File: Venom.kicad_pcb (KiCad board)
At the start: 2 copper layers, 72 x 42 mm, 38 parts, among them CN1 HC-XH-5A-G, CN2 HC-PH-8A-G, CN3 HC-XH-8A-G, CN4 HC-XH-8A-G, CN5 HC-XH-2A-G, CN6 HC-PH-7A-G, SW1 GT-TC030A-H020-L1N, SW2 GT-TC030A-H020-L1N, SW3 GT-TC030A-H020-L1N, U1 TLV73333PDBV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

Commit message: Potentially finished RP2040
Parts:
- moved SW1 27.1 mm to (106.7, 101.6)
- moved Y1 24.4 mm to (116.7, 96.0), turned to 180 degrees
- moved C2 16.5 mm to (119.4, 95.2), turned to -90 degrees
- moved C12 16.3 mm to (125.7, 101.6), turned to -90 degrees
- moved C13 15.5 mm to (125.7, 90.9), turned to 90 degrees
- moved C7 14.1 mm to (120.2, 98.7), turned to 180 degrees
- moved C3 13.7 mm to (116.8, 98.3)
- moved OSHW1 8.42 mm to (81.8, 95.6)
- moved C14 8.36 mm to (120.2, 97.7), turned to 180 degrees
- moved R5 5.62 mm to (119.8, 96.7), turned to 0 degrees
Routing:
- net +1V1: track 4.23 -> 34.2 mm, vias 1 -> 2
- net GND: track 27.9 -> 47.6 mm, vias 15 -> 20
- net +3V3: track 49.3 -> 55.3 mm
- net XIN: track 0.00 -> 4.05 mm
- net XOUT: track 0.00 -> 3.22 mm
- net Net-(C3-Pad1): track 0.00 -> 2.14 mm

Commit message: Nearly all wired up?
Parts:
- U2: value W25Q128JVS -> W25Q128JVSIQTR; footprint Package_SO:SOIC-8_5.23x5.23mm_P1.27mm -> easyeda2kicad:SOIC-8_L5.3-W5.3-P1.27-LS8.0-BL
- moved SW1 40.3 mm to (146.6, 106.8), turned to 180 degrees
- moved CN5 34.1 mm to (114.2, 80.0), turned to 90 degrees
- moved C12 7.82 mm to (119.3, 106.1), turned to 180 degrees
- moved CN3 4.69 mm to (98.7, 78.7)
- moved CN4 0.72 mm to (128.4, 78.7)
- moved C13 0.66 mm to (125.4, 90.3)
- moved R6 0.36 mm to (141.2, 96.0)
- moved C2 0.23 mm to (119.4, 95.0)
- turned C3 to 180 degrees
- turned U2 to 180 degrees
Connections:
- U3 pad 11: LEFT -> (2P) B4
- U3 pad 12: RIGHT -> A1 (HOME)
- U3 pad 13: DOWN -> (4P) L1
- U3 pad 14: UP -> (4K) L2
- U3 pad 15: (3K) R2 -> (3P) R1
- U3 pad 16: (3P) R1 -> (3K) R2
- U3 pad 17: (4K) L2 -> LEFT
- U3 pad 18: (4P) L1 -> RIGHT
- U3 pad 2: S2 (START) -> unconnected-(U3-GPIO0-Pad2)
- U3 pad 27: (2P) B4 -> DOWN
- U3 pad 28: (1P) B3 -> UP
- U3 pad 29: (2K) B2 -> S2 (START)
- U3 pad 3: S1 (SELECT) -> unconnected-(U3-GPIO1-Pad3)
- U3 pad 30: (1K) B1 -> S1 (SELECT)
- U3 pad 31: TURBO LED -> A2 (TP/CAPTURE)
- U3 pad 32: PLED 4 -> TURBO
- U3 pad 34: PLED 3 -> LS TOGGLE
- U3 pad 35: PLED 2 -> TURBO1
- U3 pad 36: PLED 1 -> PS4 MODE
- U3 pad 37: unconnected-(U3-GPIO25-Pad37) -> TURBO LED
- U3 pad 38: unconnected-(U3-GPIO26_ADC0-Pad38) -> PLED 4
- U3 pad 39: unconnected-(U3-GPIO27_ADC1-Pad39) -> PLED 3
- U3 pad 4: A2 (TP/CAPTURE) -> unconnected-(U3-GPIO2-Pad4)
- U3 pad 40: unconnected-(U3-GPIO28_ADC2-Pad40) -> PLED 2
- U3 pad 41: unconnected-(U3-GPIO29_ADC3-Pad41) -> PLED 1
- U3 pad 5: TURBO -> unconnected-(U3-GPIO3-Pad5)
- U3 pad 6: LS TOGGLE -> unconnected-(U3-GPIO4-Pad6)
- U3 pad 7: TURBO1 -> (1K) B1
- U3 pad 8: PS4 MODE -> (2K) B2
- U3 pad 9: A1 (HOME) -> (1P) B3
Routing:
- net S2 (START): track 0.00 -> 63.9 mm, vias 0 -> 2
- net LEFT: track 0.00 -> 42.2 mm, vias 0 -> 2
- net (3K) R2: track 0.00 -> 39.6 mm
- net RIGHT: track 0.00 -> 38.9 mm, vias 0 -> 2
- net (3P) R1: track 0.00 -> 37.0 mm
- net DOWN: track 0.00 -> 33.9 mm
- net UP: track 0.00 -> 30.8 mm
- net (4K) L2: track 0.00 -> 29.9 mm
- net (4P) L1: track 0.00 -> 28.2 mm
- net S1 (SELECT): track 0.00 -> 23.1 mm
- net TURBO: track 0.00 -> 22.5 mm
- net A2 (TP/CAPTURE): track 0.00 -> 21.9 mm
- net QSPI_SS: track 4.90 -> 26.1 mm
- net (1K) B1: track 0.00 -> 20.2 mm
- net LS TOGGLE: track 0.00 -> 17.8 mm
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- removed copper zone on F.Cu, net GND
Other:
- board text added: "PS"
- board text removed: "USB1"

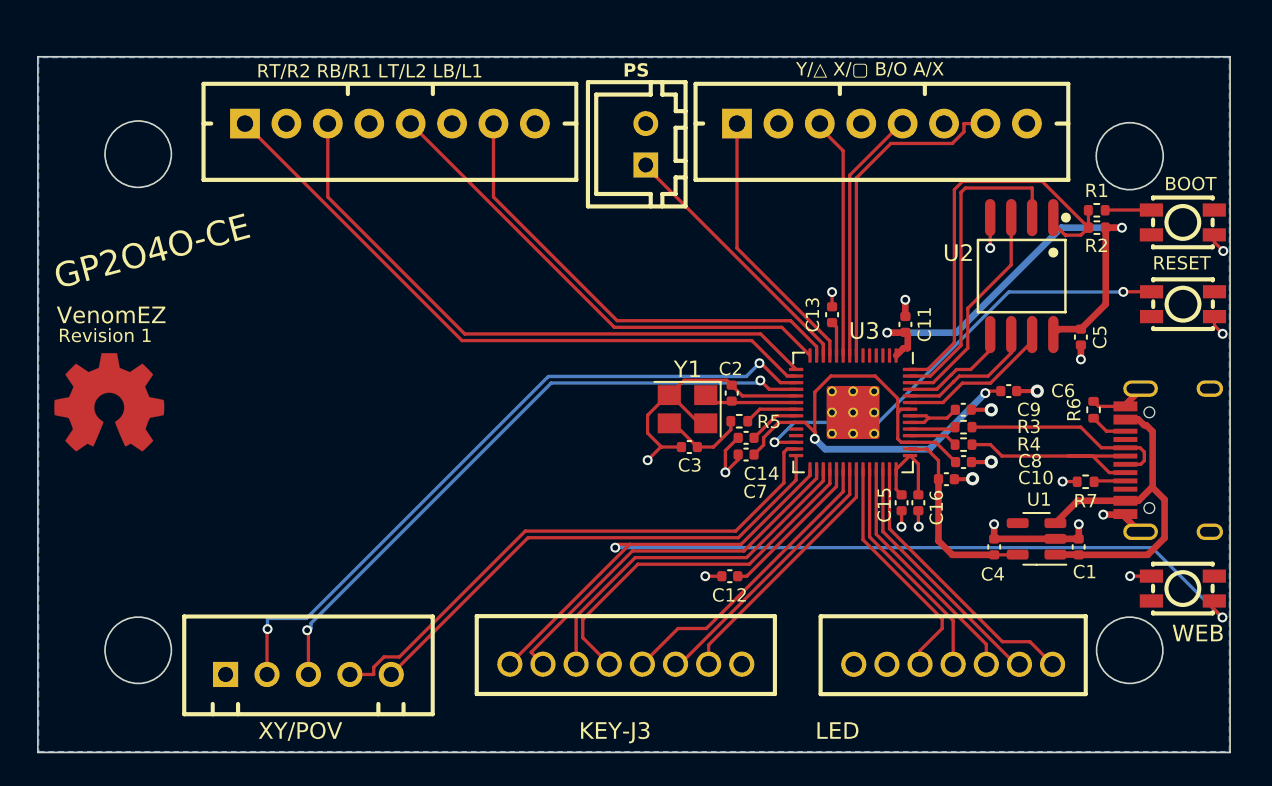
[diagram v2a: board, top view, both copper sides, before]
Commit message: Add individual up, down, left and right connectors
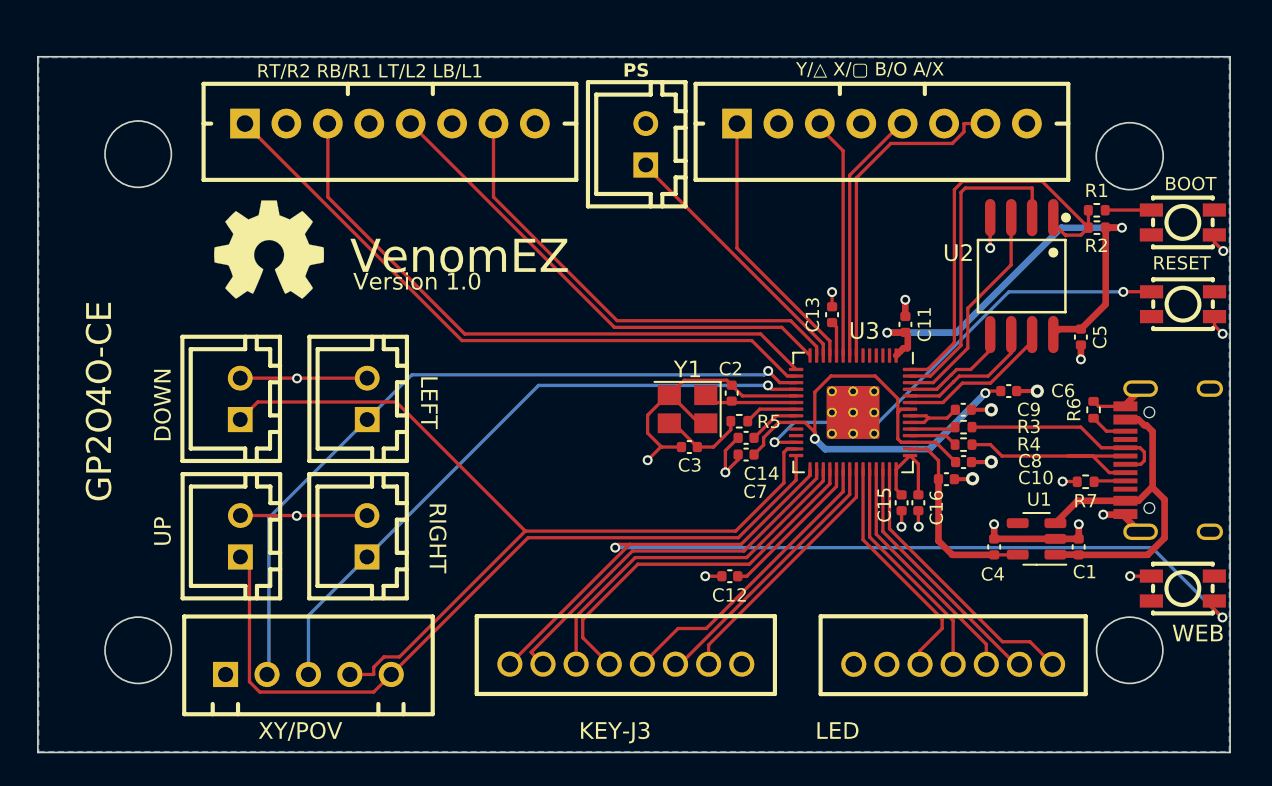
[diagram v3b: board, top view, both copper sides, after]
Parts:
- removed OSHW1: OSHW-Symbol_6.7x6mm_Copper, Symbol:OSHW-Symbol_6.7x6mm_Copper
- added CN10: HC-XH-2A-G, easyeda2kicad:CONN-TH_2P-P2.50_HC-XH-2A-G, F.Cu at (89.7, 95.4)
- added CN7: HC-XH-2A-G, easyeda2kicad:CONN-TH_2P-P2.50_HC-XH-2A-G, F.Cu at (89.7, 103.7)
- added CN8: HC-XH-2A-G, easyeda2kicad:CONN-TH_2P-P2.50_HC-XH-2A-G, F.Cu at (97.4, 95.4)
- added CN9: HC-XH-2A-G, easyeda2kicad:CONN-TH_2P-P2.50_HC-XH-2A-G, F.Cu at (97.4, 103.7)
- added REF**: OSHW-Symbol_6.7x6mm_SilkScreen, Symbol:OSHW-Symbol_6.7x6mm_SilkScreen, F.Cu at (91.4, 86.4)
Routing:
- net DOWN: track 33.9 -> 54.8 mm
- net UP: track 30.8 -> 47.8 mm
- net GND: track 50.9 -> 66.2 mm, vias 20 -> 22
- net LEFT: track 42.2 -> 45.3 mm, vias 2 -> 1
- net RIGHT: track 38.9 -> 38.8 mm, vias 2 -> 1
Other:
- board text added: "DOWN"
- board text added: "LEFT"
- board text added: "RIGHT"
- board text added: "UP"
- board text added: "Version 1.0"
- board text removed: "Revision 1"

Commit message: Update silk
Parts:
- moved REF** 1.03 mm to (91.5, 87.4)
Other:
- board text added: "Version 1.0 Powered by GP2040-CE"
- board text removed: "GP2O4O-CE"
- board text removed: "Version 1.0"

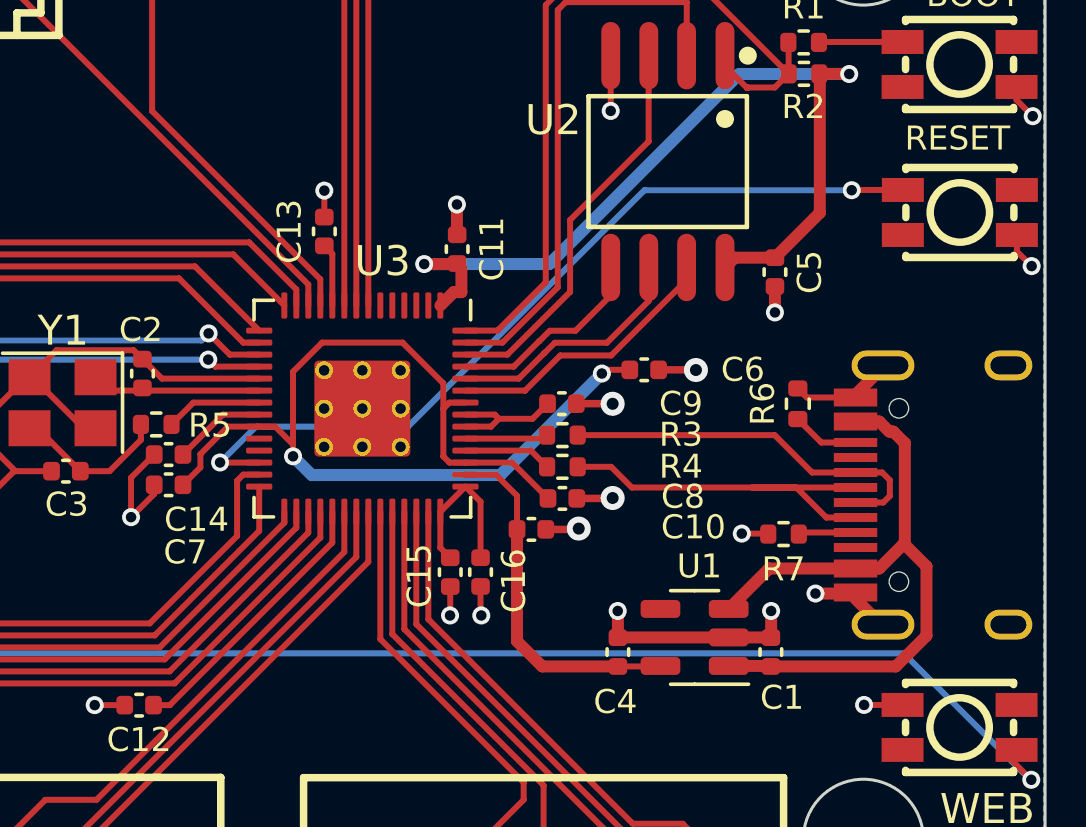
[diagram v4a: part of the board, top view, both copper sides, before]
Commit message: No DRC errors!
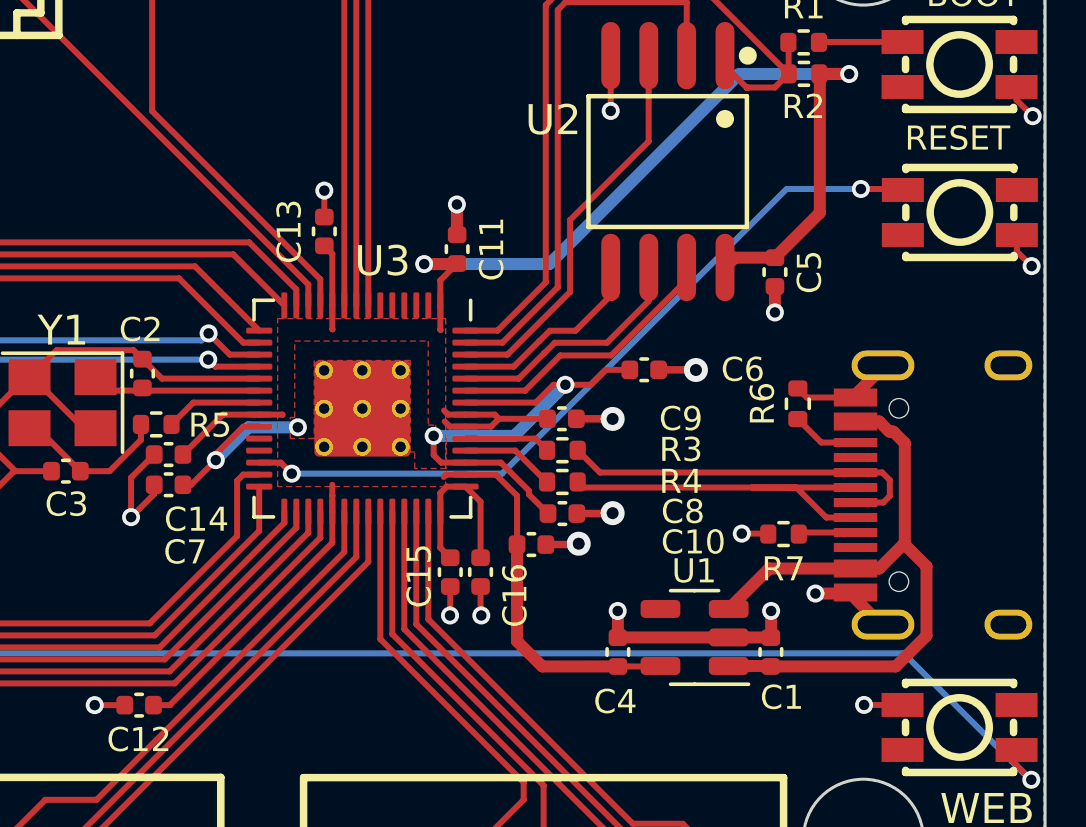
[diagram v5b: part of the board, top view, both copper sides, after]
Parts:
- moved C10 0.50 mm to (132.3, 100.7)
- moved C8 0.50 mm to (133.4, 99.7)
- moved C9 0.50 mm to (133.4, 96.5)
- moved R3 0.50 mm to (133.4, 97.6)
- moved R4 0.50 mm to (133.4, 98.6)
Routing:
- net +1V1: track 34.4 -> 23.0 mm, vias 2 -> 4
- net +3V3: track 65.4 -> 70.9 mm
- net RUN: track 27.8 -> 25.6 mm
- added copper zone on F.Cu, net +1V1
- added copper zone on F.Cu, net +3V3
